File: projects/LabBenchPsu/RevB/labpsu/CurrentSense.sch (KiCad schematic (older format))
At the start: 25 parts, among them IC1 LM358, U5 INA219

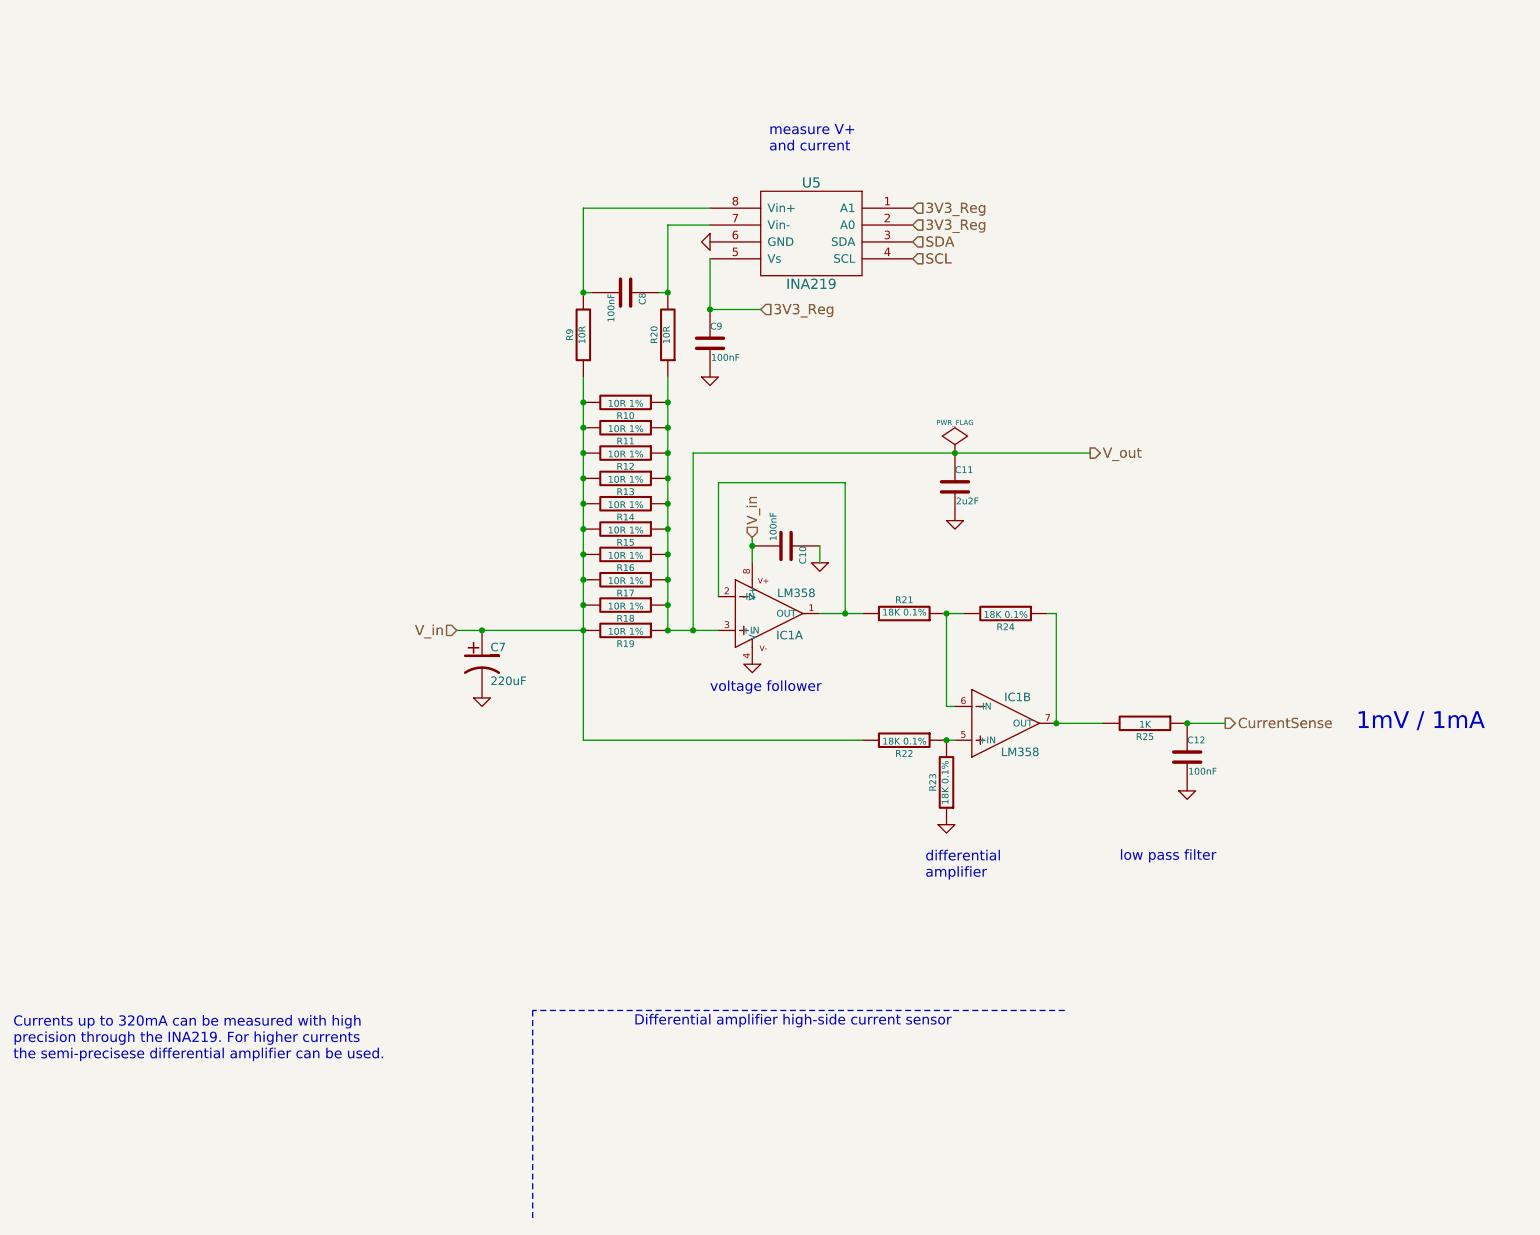
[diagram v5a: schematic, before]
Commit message: schematic with new DAC
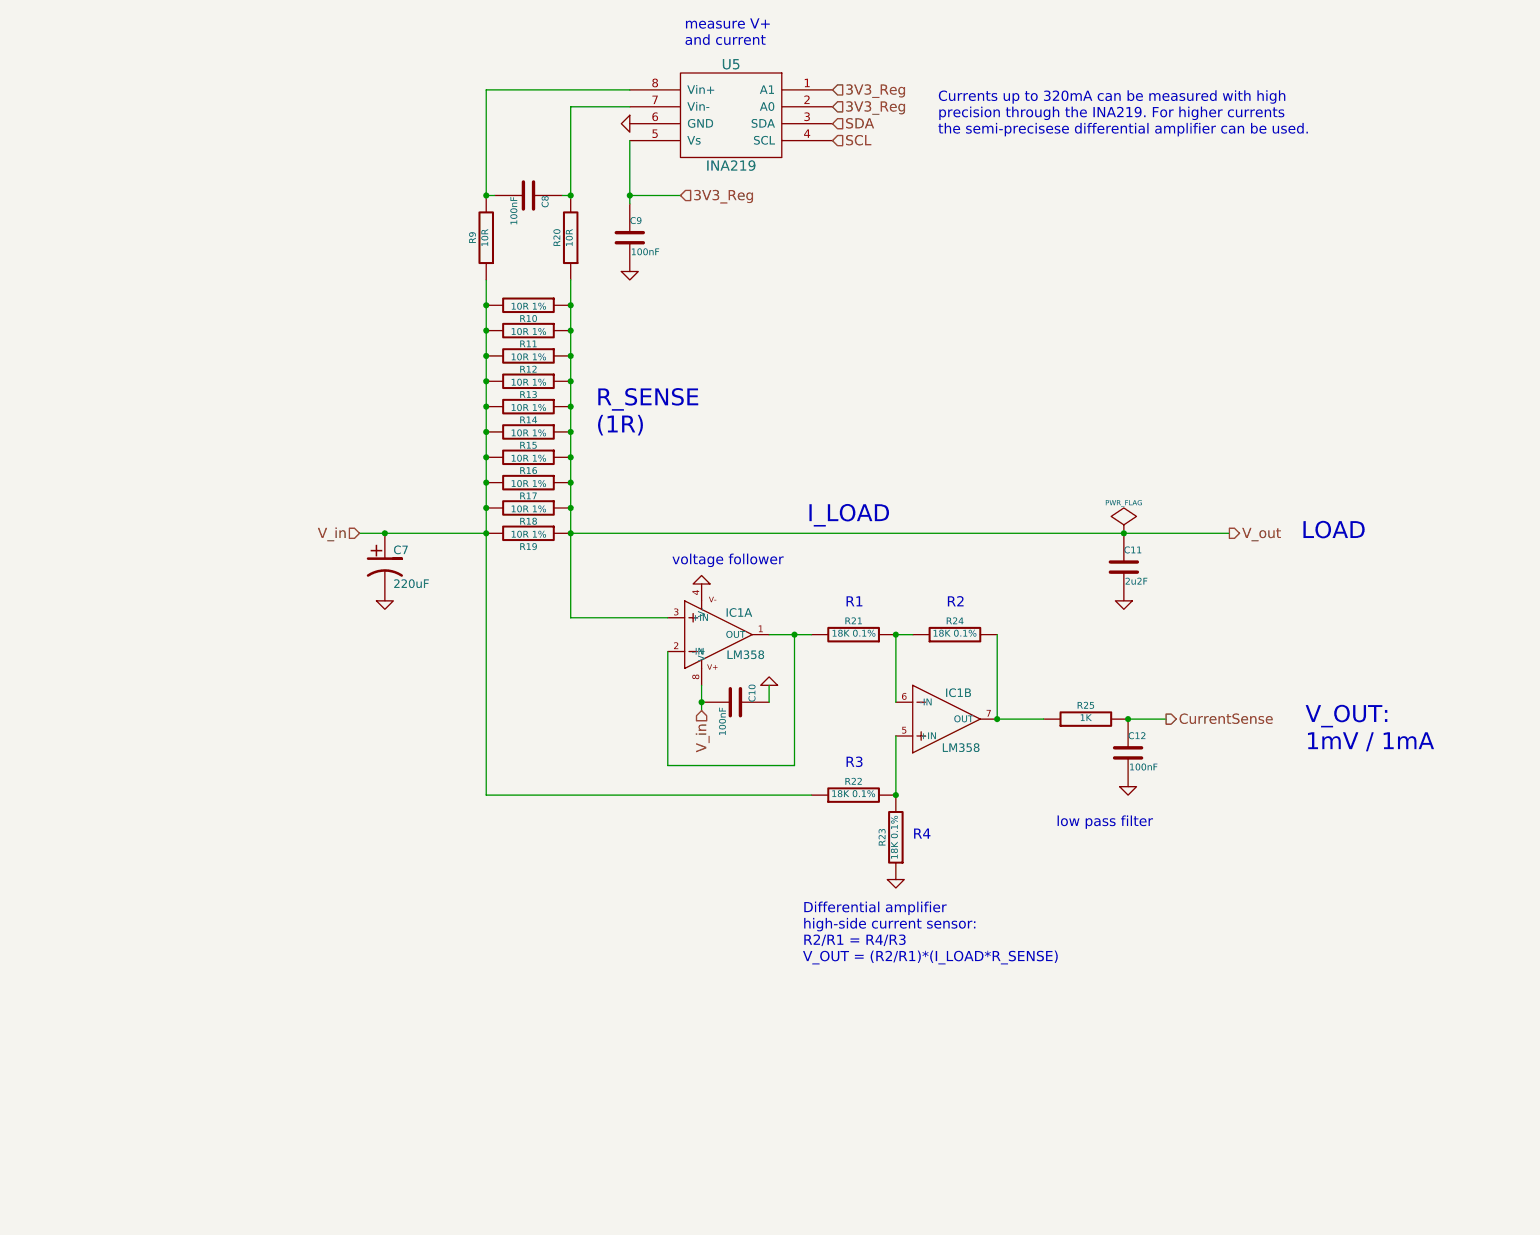
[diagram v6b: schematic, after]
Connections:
- net CurrentSense: now also R25.2; no longer R25.1
- net V_in: now also R22.1; no longer R22.2
- net at IC1.5 (+IN), R23.2: now also R22.2; no longer R22.1
- net at IC1.6 (-IN), R21.1: now also R24.1; no longer R24.2
- new net: IC1.7 (OUT), R24.2, R25.1
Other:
- note added: "Differential amplifier \nhigh-side current sensor:\nR2/R1 = R4/R3\nV_OUT = (R2/R1)*(I_LOAD*R_SENSE)"
- note added: "I_LOAD"
- note added: "LOAD"
- note added: "R1"
- note added: "R2"
- note added: "R3"
- note added: "R4"
- note added: "R_SENSE\n(1R)"
- note added: "V_OUT:\n1mV / 1mA"
- note removed: "1mV / 1mA"
- note removed: "Differential amplifier high-side current sensor"
- note removed: "differential \namplifier"
- moved on the sheet: C10, C11, C12, C7, C8, C9, IC1A, IC1B, R10, R11, R12, R13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

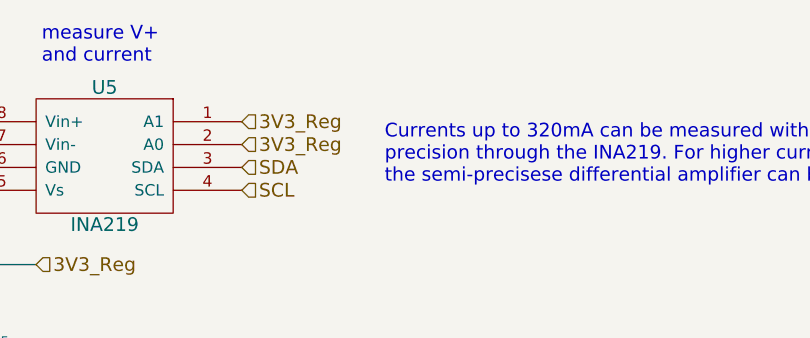
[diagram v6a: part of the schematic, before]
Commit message: i2c addresses added
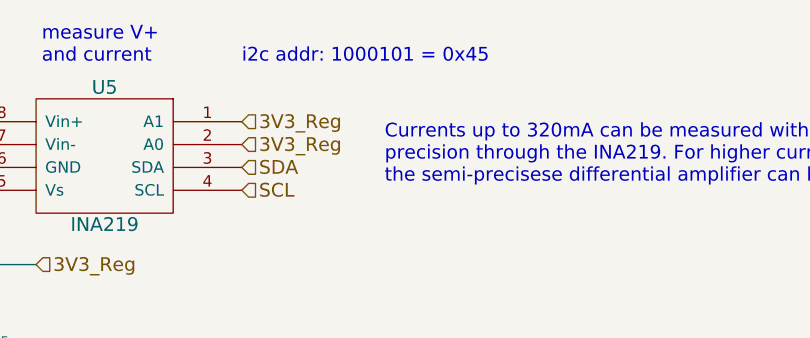
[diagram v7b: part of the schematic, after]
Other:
- note added: "i2c addr: 1000101 = 0x45"
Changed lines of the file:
@@
 Wire Wire Line
 	4025 3700 7925 3700
+Text Notes 5575 825  0    60   ~ 0
+i2c addr: 1000101 = 0x45
 $EndSCHEMATC
